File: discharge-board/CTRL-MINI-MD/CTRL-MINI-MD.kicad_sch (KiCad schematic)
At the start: 21 parts, among them J1 MD-L, J2 MD-R, U1 TMC2130-LA, U2 BD50FC0FP

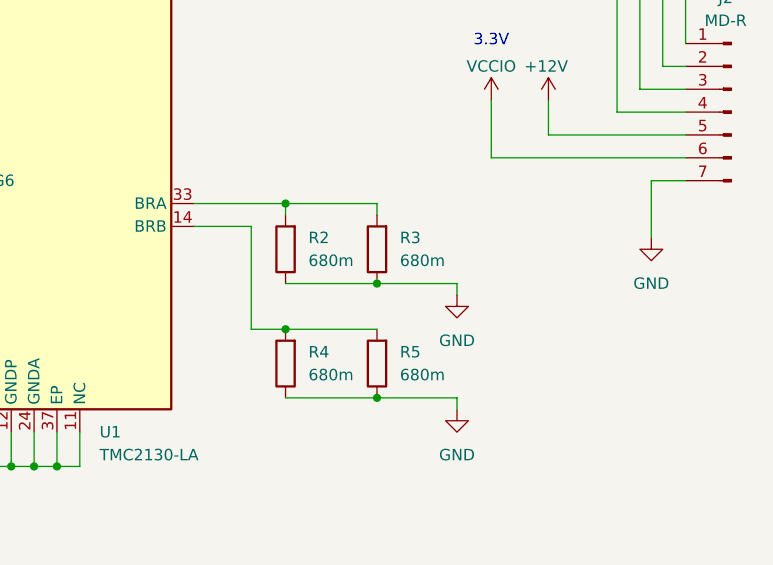
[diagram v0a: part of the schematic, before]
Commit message: Use jumper to switch 0.4A / 0.2A
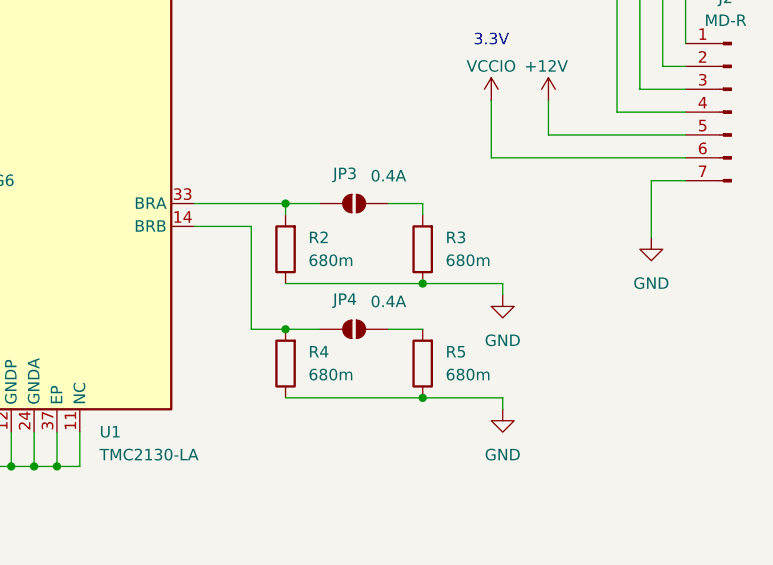
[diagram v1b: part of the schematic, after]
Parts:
- added JP3, JP4: 0.4A, symbol Jumper:SolderJumper_2_Open
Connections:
- net at R4.2, U1.14 (BRB): now also JP4.1 (A); no longer R5.2
- net at R2.2, U1.33 (BRA): now also JP3.1 (A); no longer R3.2
- new net: JP3.2 (B), R3.2
- new net: JP4.2 (B), R5.2
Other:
- moved on the sheet: R3, R5

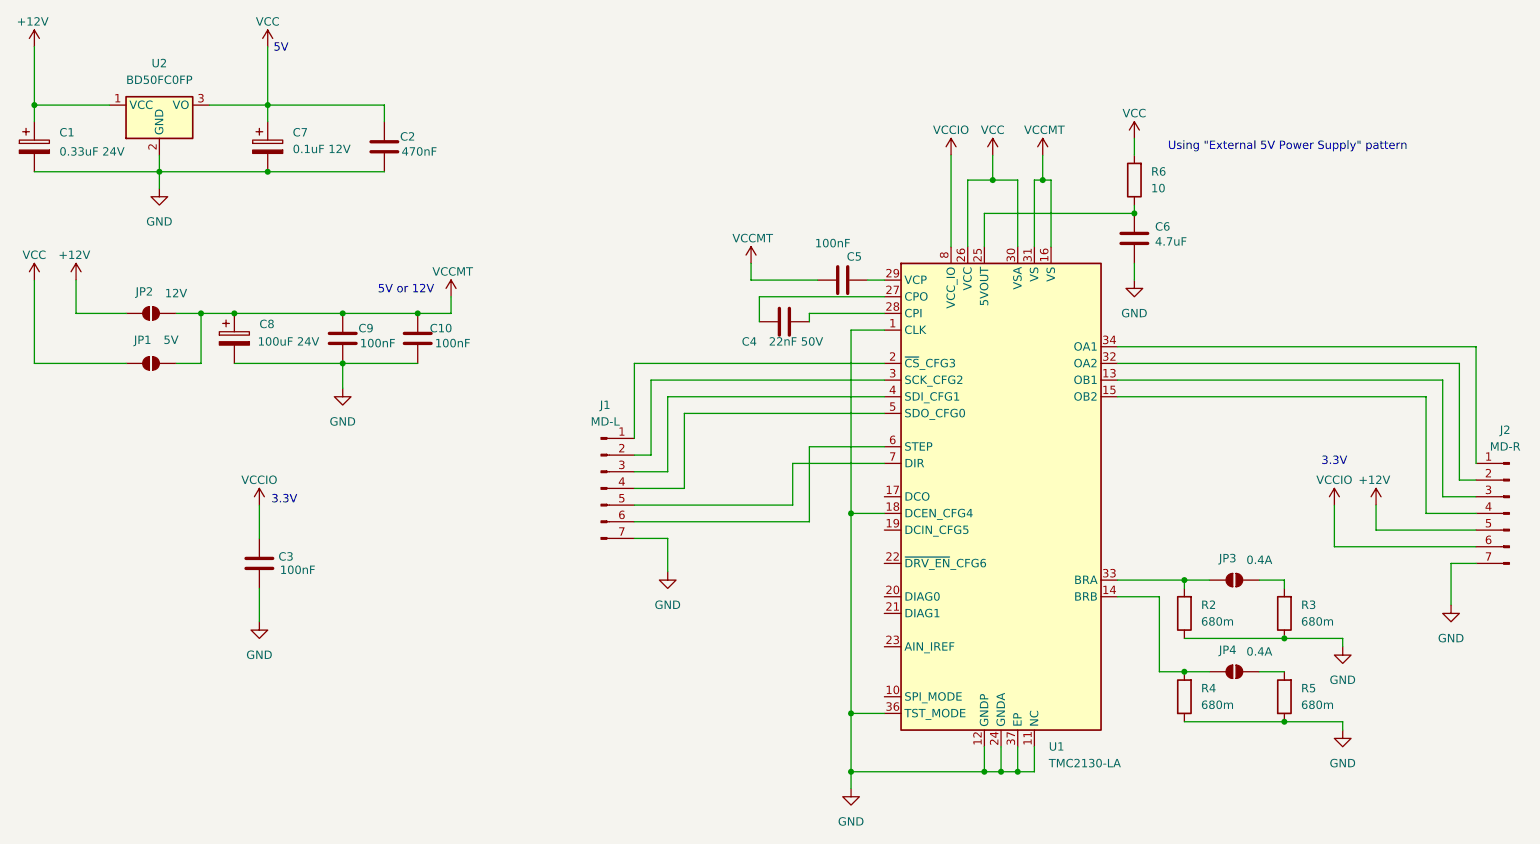
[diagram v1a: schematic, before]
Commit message: DRC-pass in MD board as 4-layer PCB
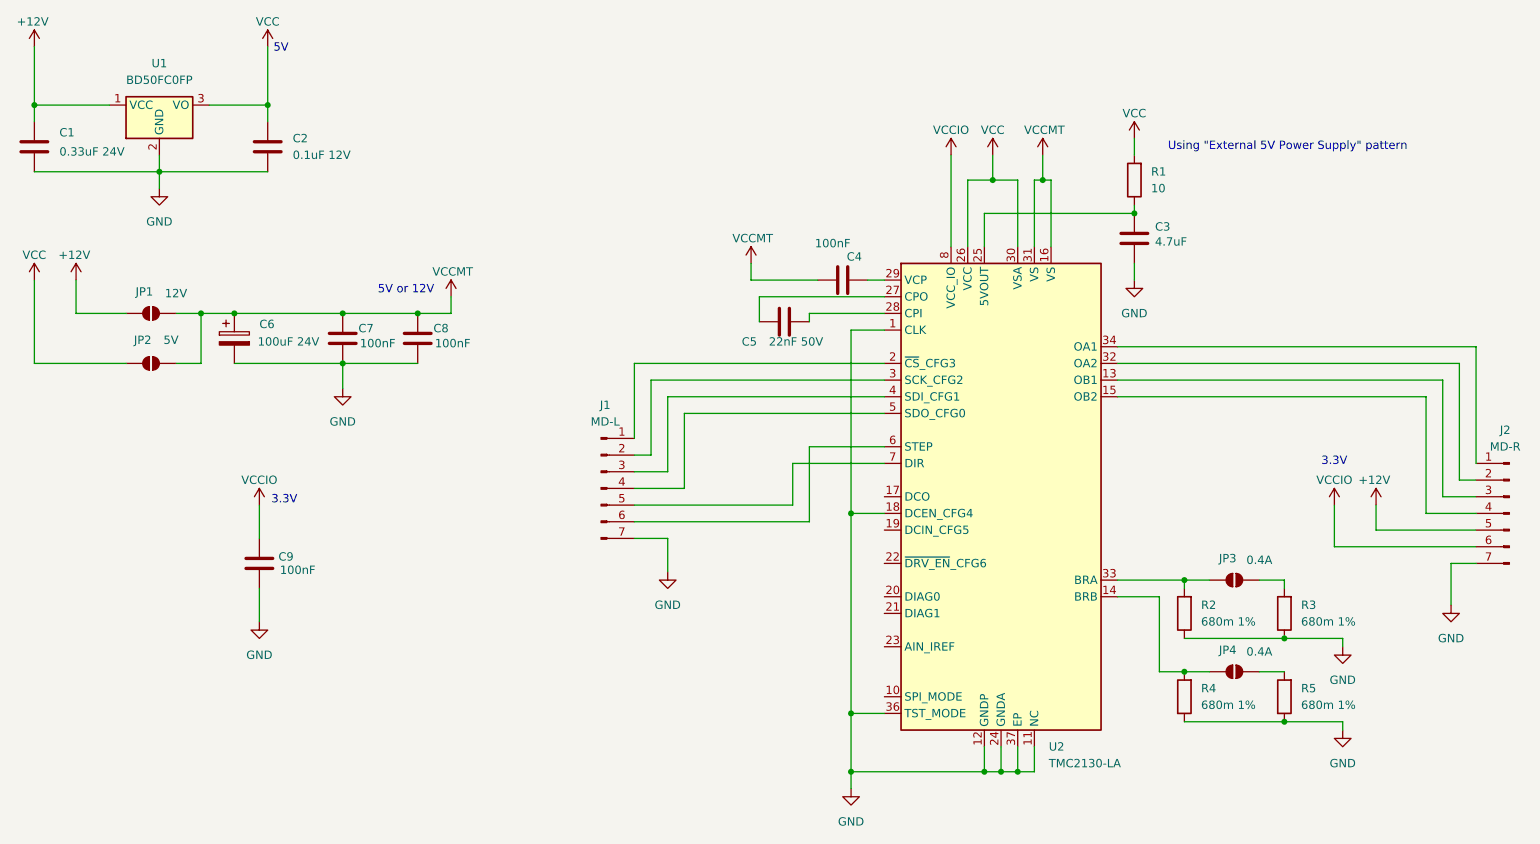
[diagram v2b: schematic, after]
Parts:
- removed C2: 470nF, symbol Device:C
- C1: footprint (none) -> Capacitor_SMD:C_0603_1608Metric; symbol Device:C_Polarized -> Device:C
- C2: renamed from C7; footprint (none) -> Capacitor_SMD:C_0603_1608Metric; symbol Device:C_Polarized -> Device:C
- C3: renamed from C6; footprint (none) -> Capacitor_SMD:C_0603_1608Metric
- C4: renamed from C5; footprint (none) -> Capacitor_SMD:C_0603_1608Metric
- C5: renamed from C4; footprint (none) -> Capacitor_SMD:C_0603_1608Metric
- C6: renamed from C8; footprint (none) -> Capacitor_THT:CP_Radial_D8.0mm_P3.50mm
- C7: renamed from C9; footprint (none) -> Capacitor_SMD:C_0603_1608Metric
- C8: renamed from C10; footprint (none) -> Capacitor_SMD:C_0603_1608Metric
- C9: renamed from C3; footprint (none) -> Capacitor_SMD:C_0603_1608Metric
- J1, J2: footprint (none) -> Connector_PinHeader_2.54mm:PinHeader_1x07_P2.54mm_Vertical
- JP1: renamed from JP2; footprint (none) -> Jumper:SolderJumper-2_P1.3mm_Open_RoundedPad1.0x1.5mm
- JP2: renamed from JP1; footprint (none) -> Jumper:SolderJumper-2_P1.3mm_Open_RoundedPad1.0x1.5mm
- JP3, JP4: footprint (none) -> Jumper:SolderJumper-2_P1.3mm_Open_RoundedPad1.0x1.5mm
- R1: renamed from R6; footprint (none) -> Resistor_SMD:R_0603_1608Metric
- R2, R3, R4, R5: value 680m -> 680m 1%; footprint (none) -> Resistor_SMD:R_0603_1608Metric
- renumbered U2 to U1, U1 to U2

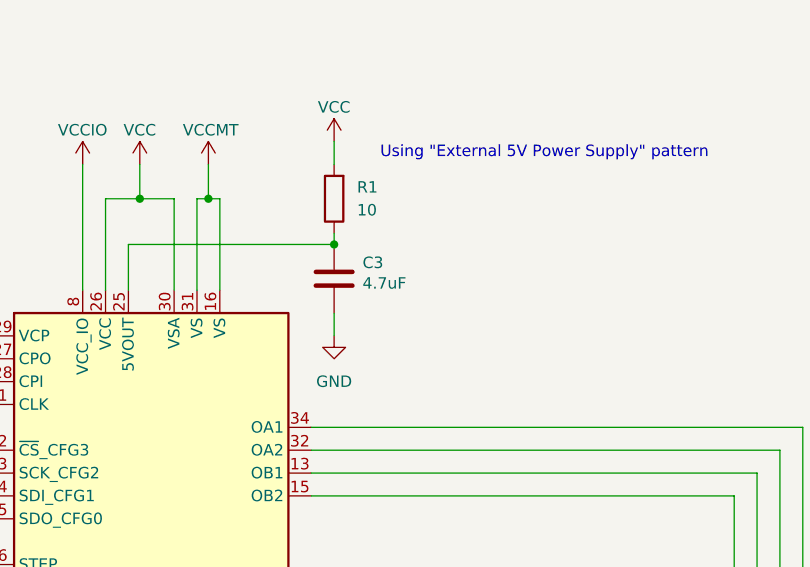
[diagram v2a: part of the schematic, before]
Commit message: Add lcsc number
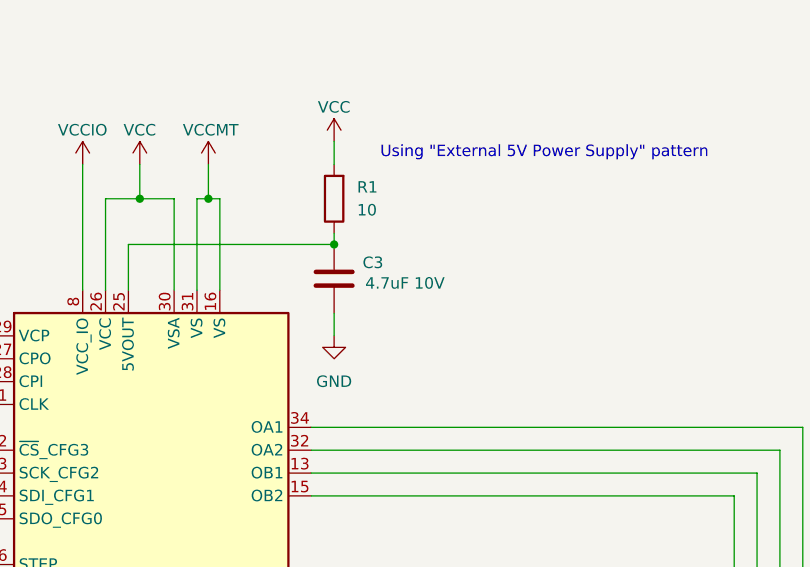
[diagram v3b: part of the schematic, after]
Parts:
- C3: value 4.7uF -> 4.7uF 10V
- U2: LCSC (none) -> C915795
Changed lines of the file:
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@@
+			)
+		)
+		(property "LCSC" "C915795"
+			(at 172.72 97.79 0)
+			(effects
+				(font
+					(size 1.27 1.27)
+				)
+				(hide yes)
 			)
 		)
@@
 		)
 		(property "Description" "Unpolarized capacitor for VCC"
+			(at 83.82 73.66 0)
+			(effects
+				(font
+					(size 1.27 1.27)
+				)
+				(hide yes)
+			)
+		)
+		(property "LCSC" ""
 			(at 83.82 73.66 0)
 			(effects
@@
 			)
 		)
+		(property "LCSC" ""
+			(at 193.04 49.53 0)
+			(effects
+				(font
+					(size 1.27 1.27)
+				)
+				(hide yes)
+			)
+		)
 		(pin "1"
 		)
@@
 			)
 		)
+		(property "LCSC" ""
+			(at 200.66 128.27 0)
+			(effects
+				(font
+					(size 1.27 1.27)
+				)
+				(hide yes)
+			)
+		)
 		(pin "1"
 		)
@@
 		)
 		(property "Description" "Solder Jumper, 2-pole, open"
+			(at 208.28 110.49 0)
+			(effects
+				(font
+					(size 1.27 1.27)
+				)
+				(hide yes)
+			)
+		)
+		(property "LCSC" ""
 			(at 208.28 110.49 0)
 			(effects
@@
 			)
 		)
+		(property "LCSC" ""
+			(at 250.19 100.33 0)
+			(effects
+				(font
+					(size 1.27 1.27)
+				)
+				(hide yes)
+			)
+		)
 		(pin "2"
 		)
@@
 			)
 		)
+		(property "LCSC" ""
+			(at 72.39 73.66 0)
+			(effects
+				(font
+					(size 1.27 1.27)
+				)
+				(hide yes)
+			)
+		)
 		(pin "1"
 		)
@@
 		)
 		(property "Description" "Unpolarized capacitor"
+			(at 139.7 71.12 0)
+			(effects
+				(font
+					(size 1.27 1.27)
+				)
+				(hide yes)
+			)
+		)
+		(property "LCSC" ""
 			(at 139.7 71.12 0)
 			(effects
@@
 			)
 		)
+		(property "LCSC" ""
+			(at 111.76 96.52 0)
+			(effects
+				(font
+					(size 1.27 1.27)
+				)
+				(hide yes)
+			)
+		)
 		(pin "2"
 		)
@@
 			)
 		)
+		(property "LCSC" ""
+			(at 215.9 115.57 0)
+			(effects
+				(font
+					(size 1.27 1.27)
+				)
+				(hide yes)
+			)
+		)
 		(pin "1"
 		)
@@
 			)
 		)
+		(property "LCSC" ""
+			(at 200.66 115.57 0)
+			(effects
+				(font
+					(size 1.27 1.27)
+				)
+				(hide yes)
+			)
+		)
 		(pin "1"
 		)
@@
 		)
 		(property "Description" "Polarized capacitor"
+			(at 55.88 73.66 0)
+			(effects
+				(font
+					(size 1.27 1.27)
+				)
+				(hide yes)
+			)
+		)
+		(property "LCSC" ""
 			(at 55.88 73.66 0)
 			(effects
@@
 			)
 		)
-		(property "Value" "4.7uF"
-			(at 198.628 58.928 0)
+		(property "Value" "4.7uF 10V"
+			(at 200.914 58.928 0)
 			(effects
 				(font
@@
 		)
 		(property "Description" "Unpolarized capacitor"
+			(at 193.04 58.42 0)
+			(effects
+				(font
+					(size 1.27 1.27)
+				)
+				(hide yes)
+			)
+		)
+		(property "LCSC" ""
 			(at 193.04 58.42 0)
 			(effects
@@
 			)
 		)
+		(property "LCSC" ""
+			(at 44.45 38.1 0)
+			(effects
+				(font
+					(size 1.27 1.27)
+				)
+				(hide yes)
+			)
+		)
 		(pin "1"
 		)
@@
 			)
 		)
+		(property "LCSC" ""
+			(at 59.69 107.95 0)
+			(effects
+				(font
+					(size 1.27 1.27)
+				)
+				(hide yes)
+			)
+		)
 		(pin "1"
 		)
@@
 		)
 		(property "Description" "Solder Jumper, 2-pole, open"
+			(at 43.18 69.85 0)
+			(effects
+				(font
+					(size 1.27 1.27)
+				)
+				(hide yes)
+			)
+		)
+		(property "LCSC" ""
 			(at 43.18 69.85 0)
 			(effects
@@
 			)
 		)
+		(property "LCSC" ""
+			(at 60.96 44.45 0)
+			(effects
+				(font
+					(size 1.27 1.27)
+				)
+				(hide yes)
+			)
+		)
 		(pin "2"
 		)
@@
 		)
 		(property "Description" "Unpolarized capacitor"
+			(at 148.59 64.77 0)
+			(effects
+				(font
+					(size 1.27 1.27)
+				)
+				(hide yes)
+			)
+		)
+		(property "LCSC" ""
 			(at 148.59 64.77 0)
 			(effects
@@
 			)
 		)
+		(property "LCSC" ""
+			(at 208.28 124.46 0)
+			(effects
+				(font
+					(size 1.27 1.27)
+				)
+				(hide yes)
+			)
+		)
 		(pin "1"
 		)
@@
 			)
 		)
+		(property "LCSC" ""
+			(at 215.9 128.27 0)
+			(effects
+				(font
+					(size 1.27 1.27)
+				)
+				(hide yes)
+			)
+		)
 		(pin "1"
 		)
@@
 			)
 		)
+		(property "LCSC" ""
+			(at 43.18 77.47 0)
+			(effects
+				(font
+					(size 1.27 1.27)
+				)
+				(hide yes)
+			)
+		)
 		(pin "1"
 		)
@@
 			(at 25.4 44.45 0)
 			(effects
+				(font
+					(size 1.27 1.27)
+				)
+				(hide yes)
+			)
+		)
+		(property "LCSC" ""
+			(at 25.4 44.45 0)
+			(effects
